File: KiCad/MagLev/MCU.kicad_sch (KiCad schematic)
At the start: 70 parts, among them J2 Programming header, J4 USB_B_Micro, Q1 ZX5T851GTA, Q16 TEMT7000X01, U6 ATmega328P-A, U8 FT232RL, U9 LM1117MP-5.0, Y3 J49SMH-16MHz

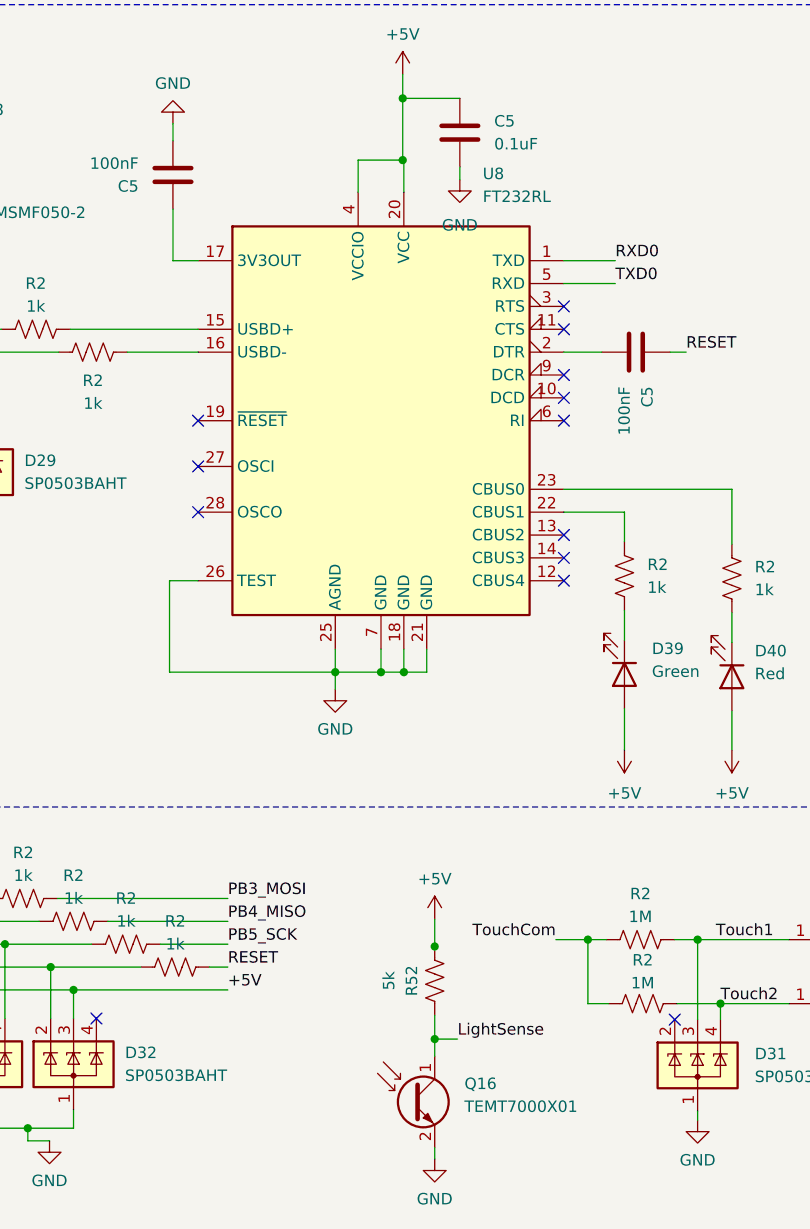
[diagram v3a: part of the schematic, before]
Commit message: Review all footprints.
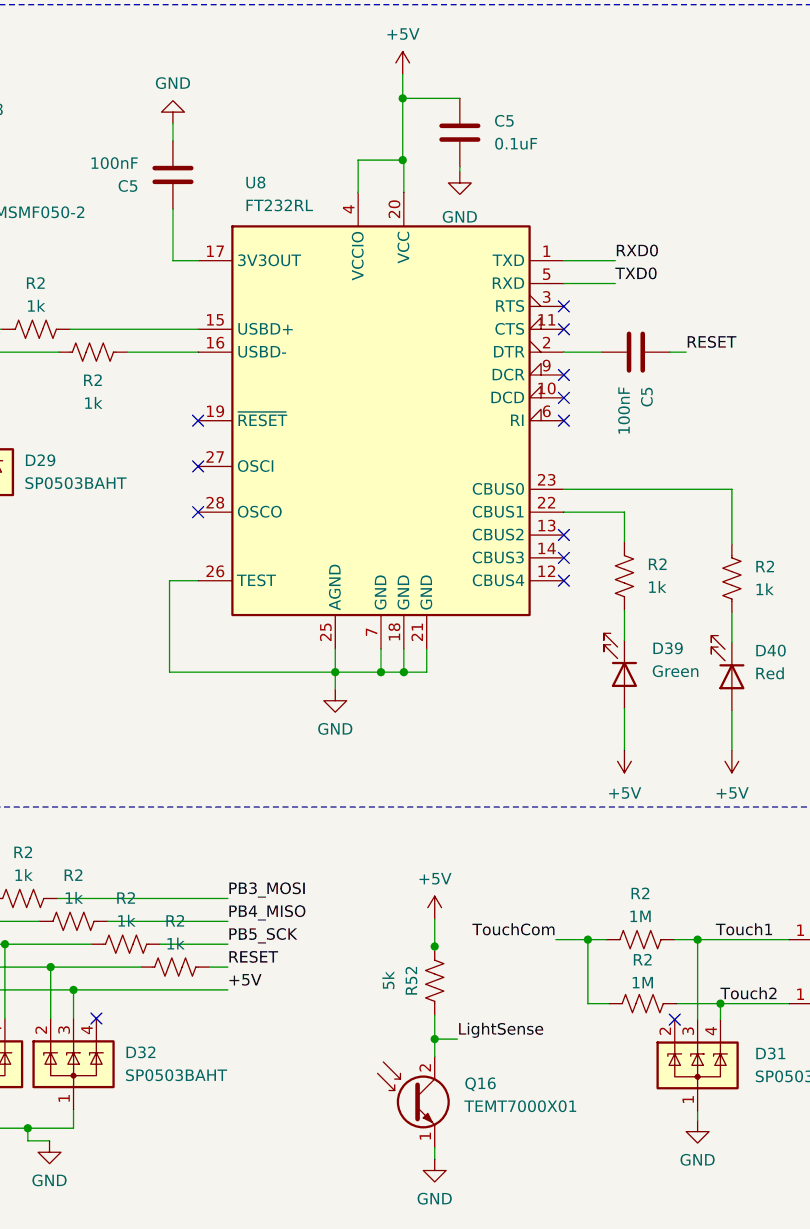
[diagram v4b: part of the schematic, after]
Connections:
- net GND: now also Q16.1 (E); no longer Q16.2 (E)
- net LightSense: now also Q16.2 (C); no longer Q16.1 (C)
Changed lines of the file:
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@@
     (stroke (width 0) (type default))
   )
-  (wire (pts (xy 98.044 66.294) (xy 98.044 67.691))
+  (wire (pts (xy 98.044 66.294) (xy 98.044 66.802))
     (stroke (width 0) (type default))
   )
@@
   (symbol (lib_id "Interface_USB:FT232RL") (at 89.281 94.488 0) (unit 1)
     (in_bom yes) (on_board yes) (dnp no)
-    (property "Reference" "U8" (at 100.584 67.056 0)
-      (effects (font (size 1.27 1.27)) (justify left))
-    )
-    (property "Value" "FT232RL" (at 100.584 69.596 0)
+    (property "Reference" "U8" (at 74.168 68.072 0)
+      (effects (font (size 1.27 1.27)) (justify left))
+    )
+    (property "Value" "FT232RL" (at 74.168 70.612 0)
       (effects (font (size 1.27 1.27)) (justify left))
     )
@@
       (effects (font (size 1.27 1.27)) hide)
     )
-    (pin "1")
-    (pin "2")
+    (pin "2")
+    (pin "1")
     (instances
       (project "MagLev"
@@
     )
   )
-  (symbol (lib_id "power:GND") (at 98.044 67.691 0) (unit 1)
-    (in_bom yes) (on_board yes) (dnp no) (fields_autoplaced)
-    (property "Reference" "#PWR038" (at 98.044 74.041 0)
-      (effects (font (size 1.27 1.27)) hide)
-    )
-    (property "Value" "GND" (at 98.044 72.771 0)
-      (effects (font (size 1.27 1.27)))
-    )
-    (property "Footprint" "" (at 98.044 67.691 0)
-      (effects (font (size 1.27 1.27)) hide)
-    )
-    (property "Datasheet" "" (at 98.044 67.691 0)
-      (effects (font (size 1.27 1.27)) hide)
-    )
+  (symbol (lib_id "power:GND") (at 98.044 66.802 0) (unit 1)
+    (in_bom yes) (on_board yes) (dnp no) (fields_autoplaced)
+    (property "Reference" "#PWR038" (at 98.044 73.152 0)
+      (effects (font (size 1.27 1.27)) hide)
+    )
+    (property "Value" "GND" (at 98.044 71.882 0)
+      (effects (font (size 1.27 1.27)))
+    )
+    (property "Footprint" "" (at 98.044 66.802 0)
+      (effects (font (size 1.27 1.27)) hide)
+    )
+    (property "Datasheet" "" (at 98.044 66.802 0)
+      (effects (font (size 1.27 1.27)) hide)
+    )

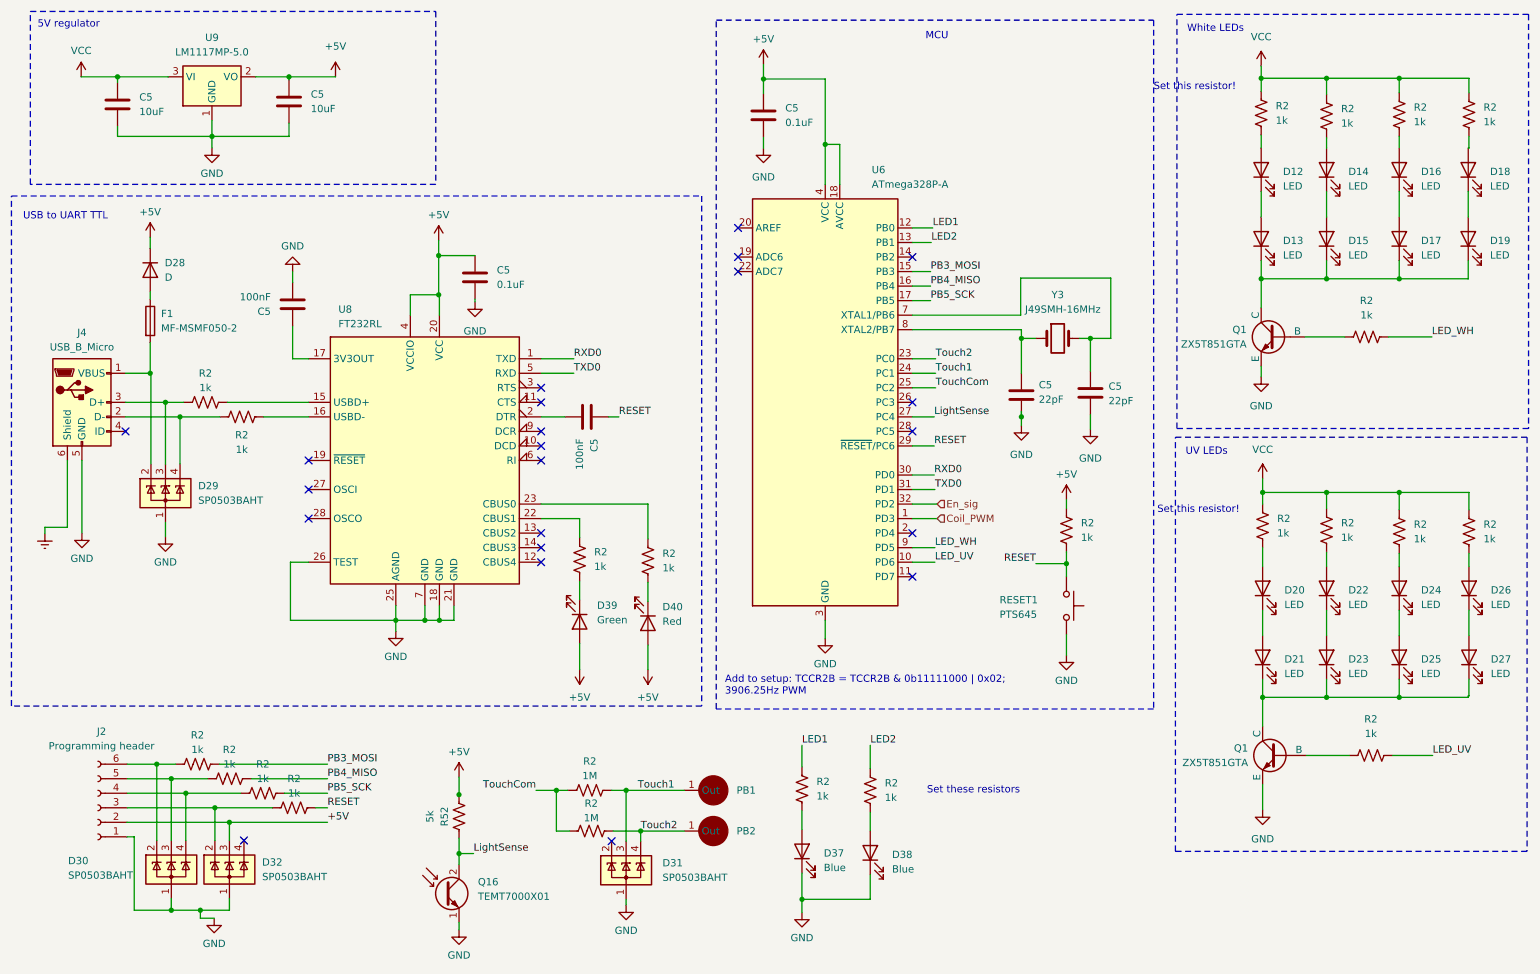
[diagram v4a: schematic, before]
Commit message: Set LED bias resistors. Move MCU status LEDs to PWM pins.
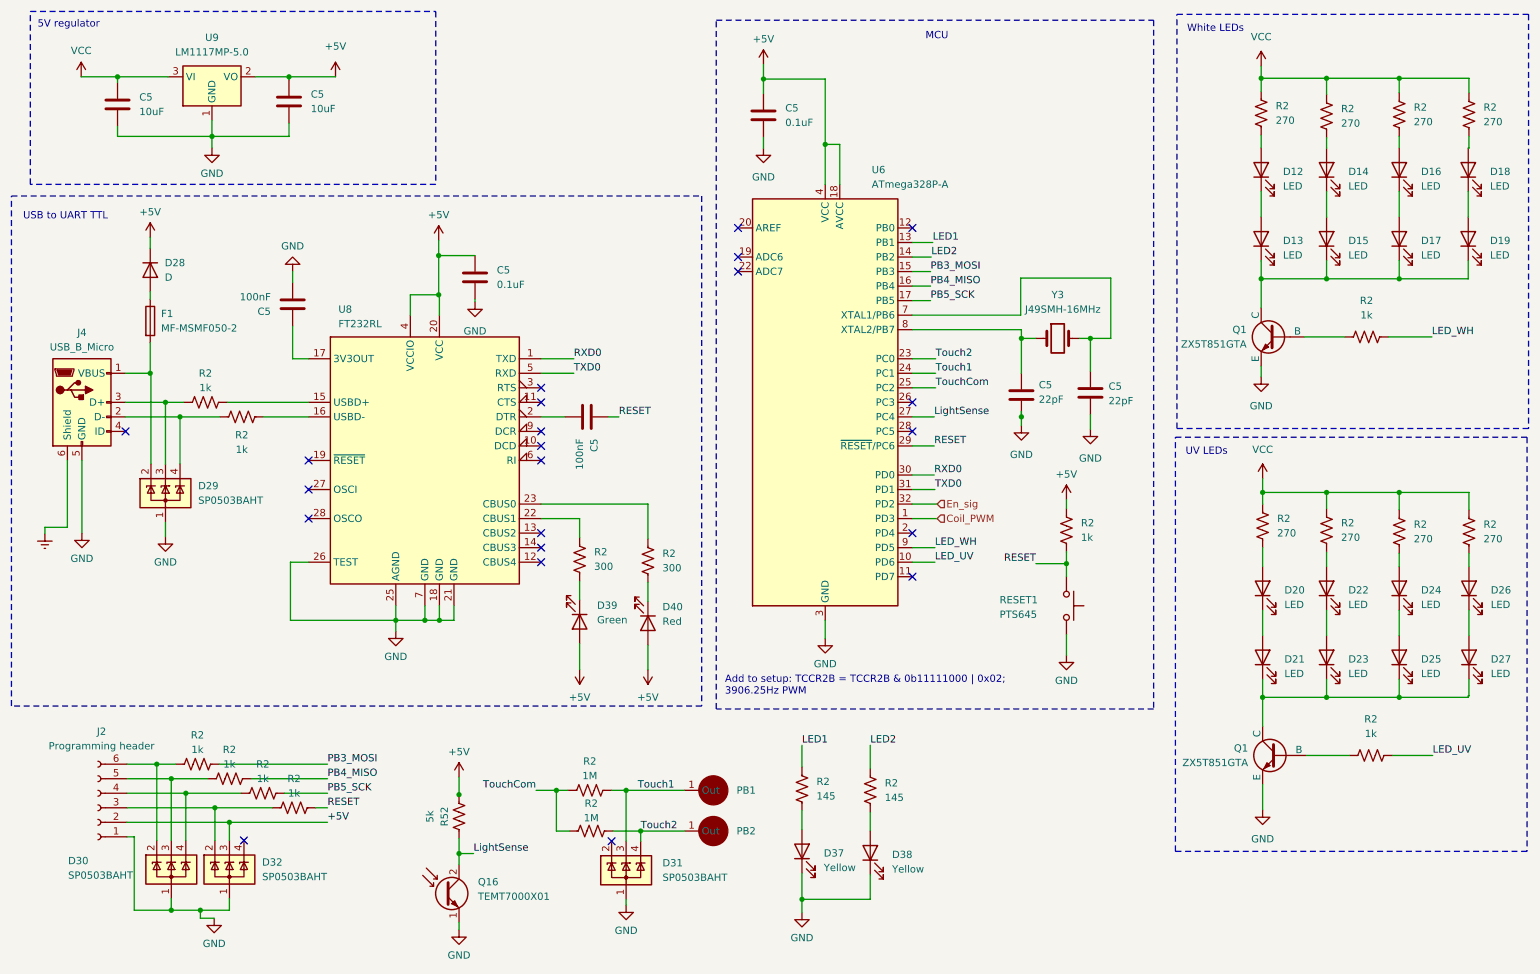
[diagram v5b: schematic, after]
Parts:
- D12, D13, D14, D15, D16, D17, D18, D19: Part (none) -> LTW-170TK
- D20: Part: (none) -> ATS2012UV415
- D21, D22, D23, D24, D25, D26, D27: Part (none) -> ATS2012UV415
- D37, D38: value Blue -> Yellow
- D39: Part (none) -> SML-LXT0805GW-TR
- D40: Part (none) -> SML-LXT0805IW-TR
- R2: value 1k -> 300
- R2: value 1k -> 270
- R2: value 1k -> 145
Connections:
- net LED1: now also U6.13 (PB1); no longer U6.12 (PB0)
- net LED2: now also U6.14 (PB2); no longer U6.13 (PB1)
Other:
- note removed: "Set these resistors"
- note removed: "Set this resistor!"
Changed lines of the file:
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@@
   (no_connect (at 121.92 161.036))
   (no_connect (at 144.018 61.468))
+  (no_connect (at 174.498 53.848))
   (no_connect (at 68.961 104.648))
   (no_connect (at 174.498 84.328))
-  (no_connect (at 174.498 58.928))
   (no_connect (at 68.961 99.568))
   (no_connect (at 109.601 109.728))
@@
     (stroke (width 0) (type default))
   )
-  (wire (pts (xy 174.498 53.848) (xy 178.054 53.848))
+  (wire (pts (xy 174.498 56.388) (xy 178.054 56.388))
     (stroke (width 0) (type default))
   )
@@
     (stroke (width 0) (type default))
   )
-  (wire (pts (xy 174.498 56.388) (xy 177.8 56.388))
+  (wire (pts (xy 174.498 58.928) (xy 177.8 58.928))
     (stroke (width 0) (type default))
   )
@@
     (fill (type none))
   )
-  (text "Set this resistor!" (at 217.297 103.886 0)
-    (effects (font (size 1.27 1.27)) (justify left bottom))
-  )
   (text "White LEDs" (at 222.504 19.812 0)
     (effects (font (size 1.27 1.27)) (justify left bottom))
   )
-  (text "Set these resistors" (at 177.038 152.908 0)
-    (effects (font (size 1.27 1.27)) (justify left bottom))
-  )
   (text "MCU" (at 176.784 21.082 0)
     (effects (font (size 1.27 1.27)) (justify left bottom))
@@
     (effects (font (size 1.27 1.27)) (justify left bottom) (href "https://forum.arduino.cc/t/varying-the-pwm-frequency-for-timer-0-or-timer-2/16679/5"))
   )
-  (text "Set this resistor!" (at 216.662 29.972 0)
-    (effects (font (size 1.27 1.27)) (justify left bottom))
-  )
   (label "TouchCom" (at 178.562 81.788 0) (fields_autoplaced)
     (effects (font (size 1.27 1.27)) (justify left bottom))
@@
     (effects (font (size 1.27 1.27)) (justify left bottom))
   )
-  (label "LED1" (at 178.054 53.848 0) (fields_autoplaced)
+  (label "LED1" (at 178.054 56.388 0) (fields_autoplaced)
     (effects (font (size 1.27 1.27)) (justify left bottom))
   )
@@
     (effects (font (size 1.27 1.27)) (justify left bottom))
   )
-  (label "LED2" (at 177.8 56.388 0) (fields_autoplaced)
+  (label "LED2" (at 177.8 58.928 0) (fields_autoplaced)
     (effects (font (size 1.27 1.27)) (justify left bottom))
   )
@@
       (effects (font (size 1.27 1.27)) (justify right))
     )
-    (property "Value" "1k" (at 118.872 113.03 0)
+    (property "Value" "300" (at 118.872 113.03 0)
       (effects (font (size 1.27 1.27)) (justify right))
     )
@@
       (effects (font (size 1.27 1.27)) (justify right))
     )
-    (property "Value" "1k" (at 249.428 107.95 0)
+    (property "Value" "270" (at 249.428 107.95 0)
       (effects (font (size 1.27 1.27)) (justify right))
     )
@@
       (effects (font (size 1.27 1.27)) (justify right))
     )
-    (property "Value" "1k" (at 249.428 35.56 0)
+    (property "Value" "270" (at 249.428 35.56 0)
       (effects (font (size 1.27 1.27)) (justify right))
     )
@@
       (effects (font (size 1.27 1.27)) (justify right))
     )
-    (property "Value" "1k" (at 169.672 153.416 0)
+    (property "Value" "145" (at 169.672 153.416 0)
       (effects (font (size 1.27 1.27)) (justify right))
     )
@@
       (effects (font (size 1.27 1.27)) hide)
     )
+    (property "Part" "LTW-170TK" (at 259.588 43.688 90)
+      (effects (font (size 1.27 1.27)) hide)
+    )
     (pin "1")
     (pin "2")
@@
       (effects (font (size 1.27 1.27)) hide)
     )
+    (property "Part" "LTW-170TK" (at 259.588 55.753 90)
+      (effects (font (size 1.27 1.27)) hide)
+    )
     (pin "1")
     (pin "2")
@@
       (effects (font (size 1.27 1.27)) hide)
     )
+    (property "Part" "ATS2012UV415" (at 246.888 116.84 90)
+      (effects (font (size 1.27 1.27)) hide)
+    )
     (pin "1")
     (pin "2")
@@
       (effects (font (size 1.27 1.27)) (justify right))
     )
-    (property "Value" "1k" (at 262.128 108.204 0)
+    (property "Value" "270" (at 262.128 108.204 0)
       (effects (font (size 1.27 1.27)) (justify right))
     )
@@
       (effects (font (size 1.27 1.27)) (justify right))
     )
-    (property "Value" "Blue" (at 159.004 165.6715 90)
+    (property "Value" "Yellow" (at 159.004 165.6715 90)
       (effects (font (size 1.27 1.27)) (justify right))
     )
@@
       (effects (font (size 1.27 1.27)) hide)
     )
+    (property "Part:" "ATS2012UV415" (at 235.712 116.84 90)
+      (effects (font (size 1.27 1.27)) hide)
+    )
     (pin "1")
     (pin "2")
@@
       (effects (font (size 1.27 1.27)) hide)
     )
+    (property "Part" "LTW-170TK" (at 235.458 55.753 90)
+      (effects (font (size 1.27 1.27)) hide)
+    )
     (pin "1")
     (pin "2")
@@
       (effects (font (size 1.27 1.27)) hide)
     )
+    (property "Part" "LTW-170TK" (at 246.888 43.688 90)
+      (effects (font (size 1.27 1.27)) hide)
+    )
     (pin "1")
     (pin "2")
@@
       (effects (font (size 1.27 1.27)) (justify right))
     )
-    (property "Value" "1k" (at 274.32 108.204 0)
+    (property "Value" "270" (at 274.32 108.204 0)
       (effects (font (size 1.27 1.27)) (justify right))
     )
@@
       (effects (font (size 1.27 1.27)) hide)
     )
+    (property "Part" "LTW-170TK" (at 235.458 43.688 90)
+      (effects (font (size 1.27 1.27)) hide)
+    )
     (pin "1")
     (pin "2")
@@
       (effects (font (size 1.27 1.27)) (justify right))
     )
-    (property "Value" "Blue" (at 170.942 165.9255 90)
+    (property "Value" "Yellow" (at 170.942 165.9255 90)
       (effects (font (size 1.27 1.27)) (justify right))
     )
@@
       (effects (font (size 1.27 1.27)) hide)
     )
+    (property "Part" "SML-LXT0805GW-TR" (at 116.332 122.682 90)
+      (effects (font (size 1.27 1.27)) hide)
+    )
     (pin "1")
     (pin "2")
@@
       (effects (font (size 1.27 1.27)) hide)
     )
+    (property "Part" "LTW-170TK" (at 271.653 55.753 90)
+      (effects (font (size 1.27 1.27)) hide)
+    )
     (pin "1")
     (pin "2")
@@
       (effects (font (size 1.27 1.27)) hide)
     )
+    (property "Part" "LTW-170TK" (at 271.653 43.688 90)
+      (effects (font (size 1.27 1.27)) hide)
+    )
     (pin "1")
     (pin "2")
@@
       (effects (font (size 1.27 1.27)) hide)
     )
+    (property "Part" "ATS2012UV415" (at 259.588 128.905 90)
+      (effects (font (size 1.27 1.27)) hide)
+    )
     (pin "1")
     (pin "2")
@@
       (effects (font (size 1.27 1.27)) hide)
     )
+    (property "Part" "ATS2012UV415" (at 246.888 128.905 90)
+      (effects (font (size 1.27 1.27)) hide)
+    )
     (pin "1")
     (pin "2")
@@
       (effects (font (size 1.27 1.27)) hide)
     )
+    (property "Part" "ATS2012UV415" (at 271.78 128.905 90)
+      (effects (font (size 1.27 1.27)) hide)
+    )
     (pin "1")
     (pin "2")
@@
       (effects (font (size 1.27 1.27)) hide)
     )
+    (property "Part" "LTW-170TK" (at 246.888 55.753 90)
+      (effects (font (size 1.27 1.27)) hide)
+    )
     (pin "1")
     (pin "2")
@@
       (effects (font (size 1.27 1.27)) (justify right))
     )
-    (property "Value" "1k" (at 274.32 35.306 0)
+    (property "Value" "270" (at 274.32 35.306 0)
       (effects (font (size 1.27 1.27)) (justify right))
     )
@@
       (effects (font (size 1.27 1.27)) hide)
     )
+    (property "Part" "ATS2012UV415" (at 271.78 116.84 90)
+      (effects (font (size 1.27 1.27)) hide)
+    )
     (pin "1")
     (pin "2")
@@
       (effects (font (size 1.27 1.27)) hide)
     )
+    (property "Part" "ATS2012UV415" (at 259.588 116.84 90)
+      (effects (font (size 1.27 1.27)) hide)
+    )
     (pin "1")
     (pin "2")
@@
       (effects (font (size 1.27 1.27)) (justify right))
     )
-    (property "Value" "1k" (at 238.252 107.188 0)
+    (property "Value" "270" (at 238.252 107.188 0)
       (effects (font (size 1.27 1.27)) (justify right))
     )
@@
       (effects (font (size 1.27 1.27)) (justify right))
     )
-    (property "Value" "1k" (at 157.734 153.162 0)
+    (property "Value" "145" (at 157.734 153.162 0)
       (effects (font (size 1.27 1.27)) (justify right))
     )
@@
       (effects (font (size 1.27 1.27)) (justify right))
     )
-    (property "Value" "1k" (at 130.81 113.284 0)
+    (property "Value" "300" (at 130.81 113.284 0)
       (effects (font (size 1.27 1.27)) (justify right))
     )
@@
       (effects (font (size 1.27 1.27)) hide)
     )
+    (property "Part" "SML-LXT0805IW-TR" (at 128.27 122.936 90)
+      (effects (font (size 1.27 1.27)) hide)
+    )
     (pin "1")
     (pin "2")
@@
       (effects (font (size 1.27 1.27)) hide)
     )
+    (property "Part" "ATS2012UV415" (at 235.712 128.905 90)
+      (effects (font (size 1.27 1.27)) hide)
+    )
     (pin "1")
     (pin "2")
@@
       (effects (font (size 1.27 1.27)) (justify right))
     )
-    (property "Value" "1k" (at 262.128 35.306 0)
+    (property "Value" "270" (at 262.128 35.306 0)
       (effects (font (size 1.27 1.27)) (justify right))
     )
@@
       (effects (font (size 1.27 1.27)) (justify right))
     )
-    (property "Value" "1k" (at 237.998 35.052 0)
+    (property "Value" "270" (at 237.998 35.052 0)
       (effects (font (size 1.27 1.27)) (justify right))
     )
